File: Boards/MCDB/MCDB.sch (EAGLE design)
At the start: 60 parts, among them IC1 MC33926, IC2 MC33926, IC3 MC33926, IC4 MC33926, IC5 MC33926, IC6 MC33926

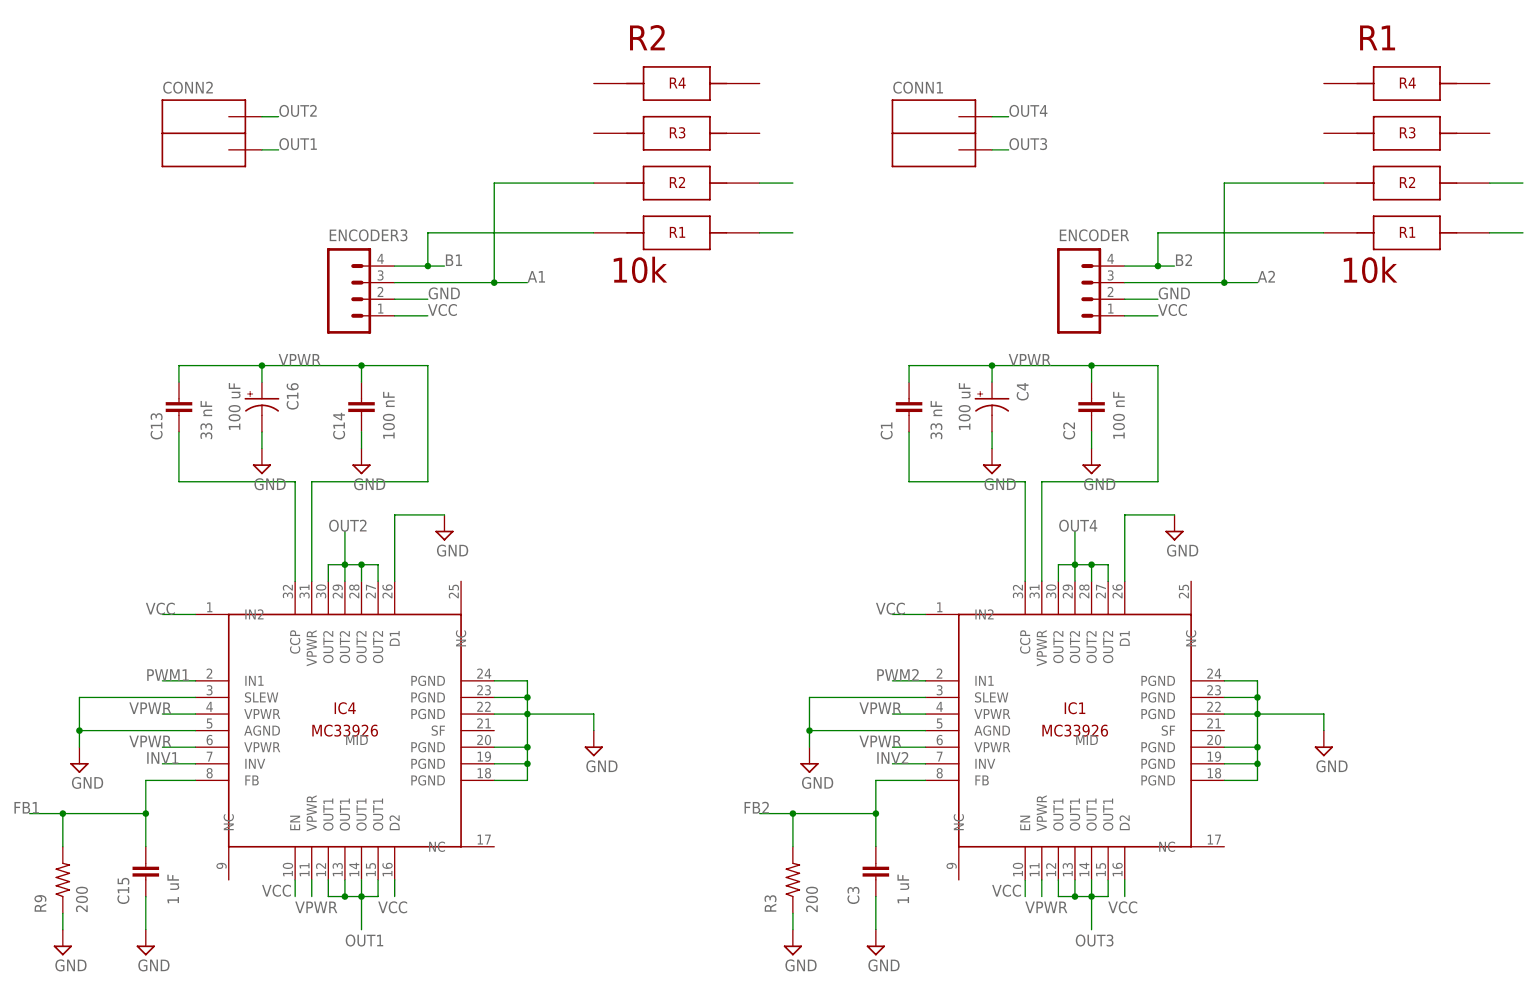
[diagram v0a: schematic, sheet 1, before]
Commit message: Started process of using new MC symbol
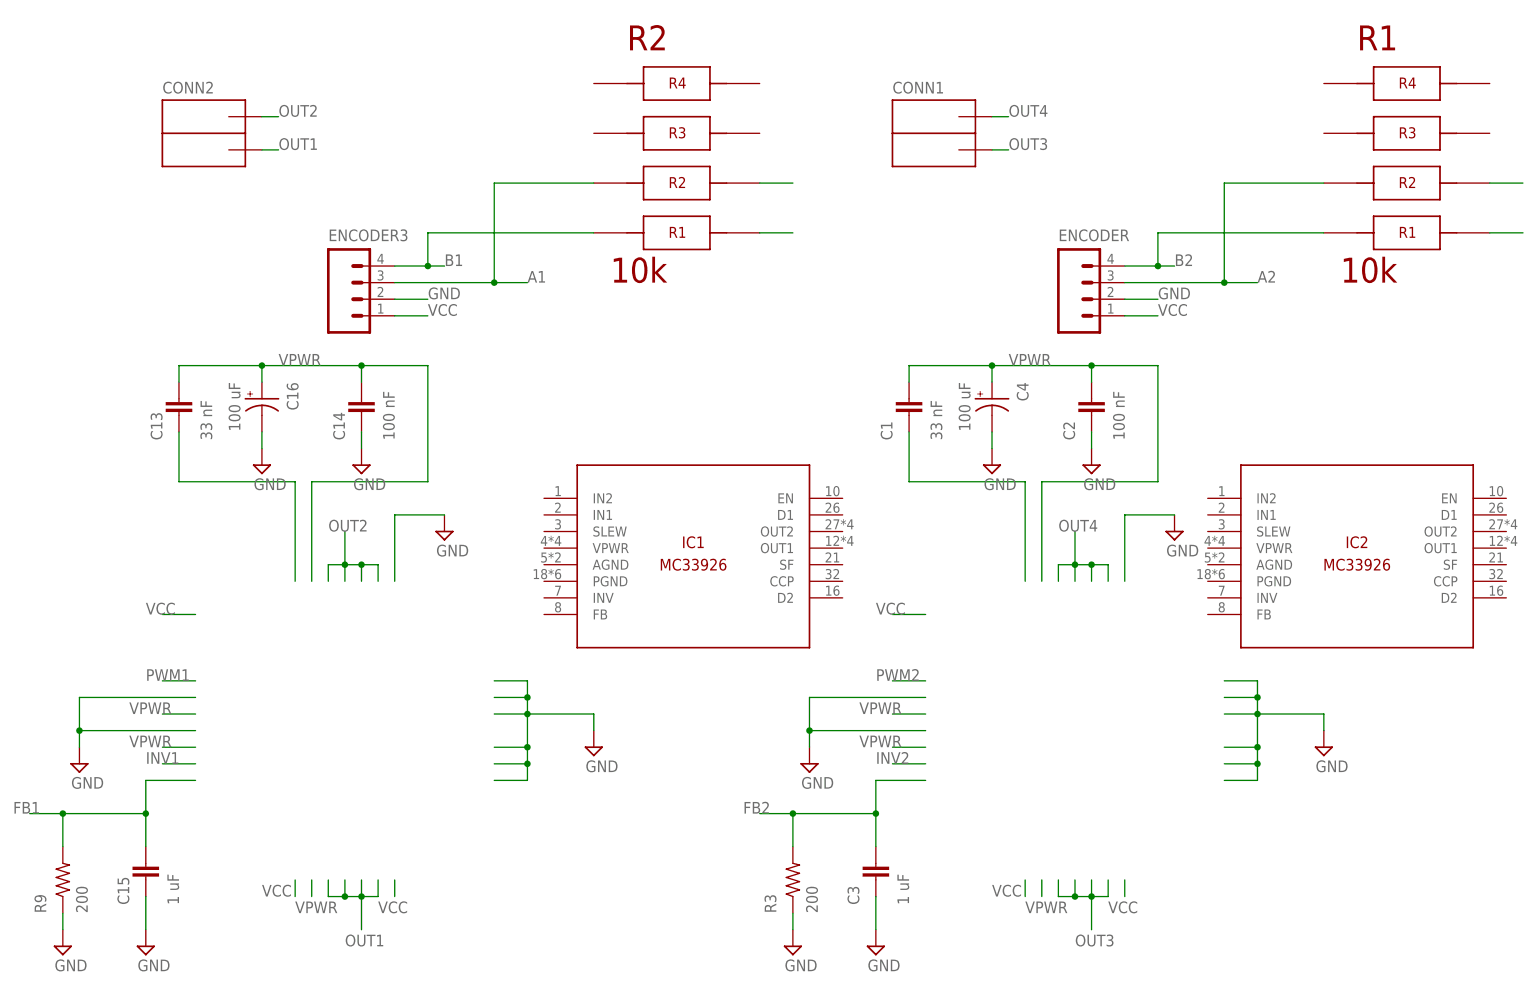
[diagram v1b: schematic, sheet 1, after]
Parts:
- removed IC3, IC4, IC5, IC6: MC33926, pie:MC33926
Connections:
- removed net INV1: IC4.INV
- removed net INV2: IC1.INV
- removed net INV3: IC2.INV
- removed net INV4: IC3.INV
- removed net INV5: IC5.INV
- removed net INV6: IC6.INV
- removed net PWM3: IC2.IN1
- removed net PWM4: IC3.IN1
- removed net PWM5: IC5.IN1
- removed net PWM6: IC6.IN1
- net CCP: no longer IC1.CCP
- net CCP1: no longer IC2.CCP
- net CCP2: no longer IC3.CCP
- net CCP3: no longer IC4.CCP
- net CCP4: no longer IC5.CCP
- net CCP5: no longer IC6.CCP
- net FB1: no longer IC4.FB
- net FB2: no longer IC1.FB
- net FB3: no longer IC2.FB
- net FB4: no longer IC3.FB
- net FB5: no longer IC5.FB
- net FB6: no longer IC6.FB
- net GND: no longer IC1.AGND, IC1.D1, IC1.PGND, IC1.PGND@1, IC1.PGND@2, IC1.PGND@3, IC1.PGND@4, IC1.PGND@5, IC1.SLEW, IC2.AGND, IC2.D1, IC2.PGND, IC2.PGND@1, IC2.PGND@2, IC2.PGND@3, IC2.PGND@4, IC2.PGND@5, IC2.SLEW, IC3.AGND, IC3.D1, IC3.PGND, IC3.PGND@1, IC3.PGND@2, IC3.PGND@3, IC3.PGND@4, IC3.PGND@5, IC3.SLEW, IC4.AGND, IC4.D1, IC4.PGND, IC4.PGND@1, IC4.PGND@2, IC4.PGND@3, IC4.PGND@4, IC4.PGND@5, IC4.SLEW, IC5.AGND, IC5.D1, IC5.PGND, IC5.PGND@1, IC5.PGND@2, IC5.PGND@3, IC5.PGND@4, IC5.PGND@5, IC5.SLEW, IC6.AGND, IC6.D1, IC6.PGND, IC6.PGND@1, IC6.PGND@2, IC6.PGND@3, IC6.PGND@4, IC6.PGND@5, IC6.SLEW
- net OUT1: no longer IC4.OUT1@1, IC4.OUT1@2, IC4.OUT1@3, IC4.OUT1@4
- net OUT10: no longer IC5.OUT2@1, IC5.OUT2@3, IC5.OUT2@4, IC5.OUT2@5
- net OUT11: no longer IC6.OUT1@1, IC6.OUT1@2, IC6.OUT1@3, IC6.OUT1@4
- net OUT12: no longer IC6.OUT2@1, IC6.OUT2@3, IC6.OUT2@4, IC6.OUT2@5
- net OUT2: no longer IC4.OUT2@1, IC4.OUT2@3, IC4.OUT2@4, IC4.OUT2@5
- net OUT3: no longer IC1.OUT1@1, IC1.OUT1@2, IC1.OUT1@3, IC1.OUT1@4
- net OUT4: no longer IC1.OUT2@1, IC1.OUT2@3, IC1.OUT2@4, IC1.OUT2@5
- net OUT5: no longer IC2.OUT1@1, IC2.OUT1@2, IC2.OUT1@3, IC2.OUT1@4
- net OUT6: no longer IC2.OUT2@1, IC2.OUT2@3, IC2.OUT2@4, IC2.OUT2@5
- net OUT7: no longer IC3.OUT1@1, IC3.OUT1@2, IC3.OUT1@3, IC3.OUT1@4
- net OUT8: no longer IC3.OUT2@1, IC3.OUT2@3, IC3.OUT2@4, IC3.OUT2@5
- net OUT9: no longer IC5.OUT1@1, IC5.OUT1@2, IC5.OUT1@3, IC5.OUT1@4
- net PWM1: no longer IC4.IN1
- net PWM2: no longer IC1.IN1
- net VCC: no longer IC1.D2, IC1.EN, IC1.IN2, IC2.D2, IC2.EN, IC2.IN2, IC3.D2, IC3.EN, IC3.IN2, IC4.D2, IC4.EN, IC4.IN2, IC5.D2, IC5.EN, IC5.IN2, IC6.D2, IC6.EN, IC6.IN2
- net VPWR: no longer IC1.VPWR, IC1.VPWR@1, IC1.VPWR@2, IC1.VPWR@3, IC2.VPWR, IC2.VPWR@1, IC2.VPWR@2, IC2.VPWR@3, IC3.VPWR, IC3.VPWR@1, IC3.VPWR@2, IC3.VPWR@3, IC4.VPWR, IC4.VPWR@1, IC4.VPWR@2, IC4.VPWR@3, IC5.VPWR, IC5.VPWR@1, IC5.VPWR@2, IC5.VPWR@3, IC6.VPWR, IC6.VPWR@1, IC6.VPWR@2, IC6.VPWR@3

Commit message: Started modifying motor controller board
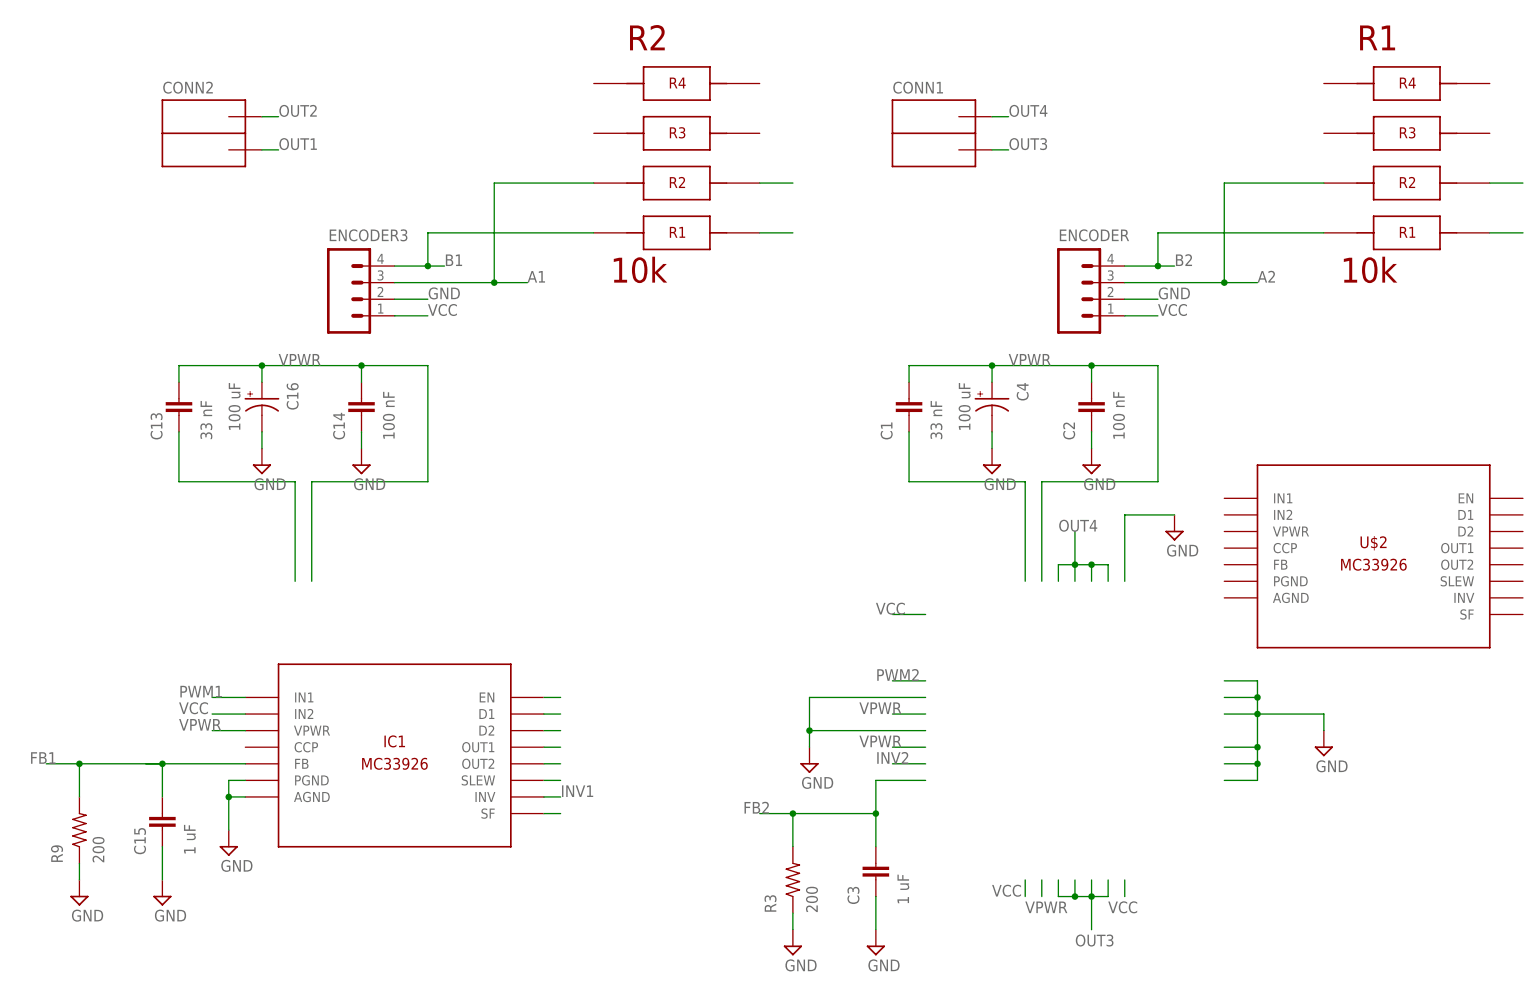
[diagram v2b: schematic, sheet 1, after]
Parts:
- removed IC2: MC33926, pie:MC33926
- added U$2, U$3, U$4, U$5, U$6: MC33926, pie:MC33926
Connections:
- new net INV1: IC1.INV
- new net N$10: IC1.SLEW
- new net N$11: IC1.SF
- new net N$2: IC1.EN
- new net N$3: IC1.D1
- new net N$6: IC1.D2
- new net N$8: IC1.OUT1
- new net N$9: IC1.OUT2
- net FB1: now also IC1.FB
- net GND: now also IC1.AGND, IC1.PGND
- net PWM1: now also IC1.IN1
- net VCC: now also IC1.IN2
- net VPWR: now also IC1.VPWR
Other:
- moved on the sheet: C15, R9

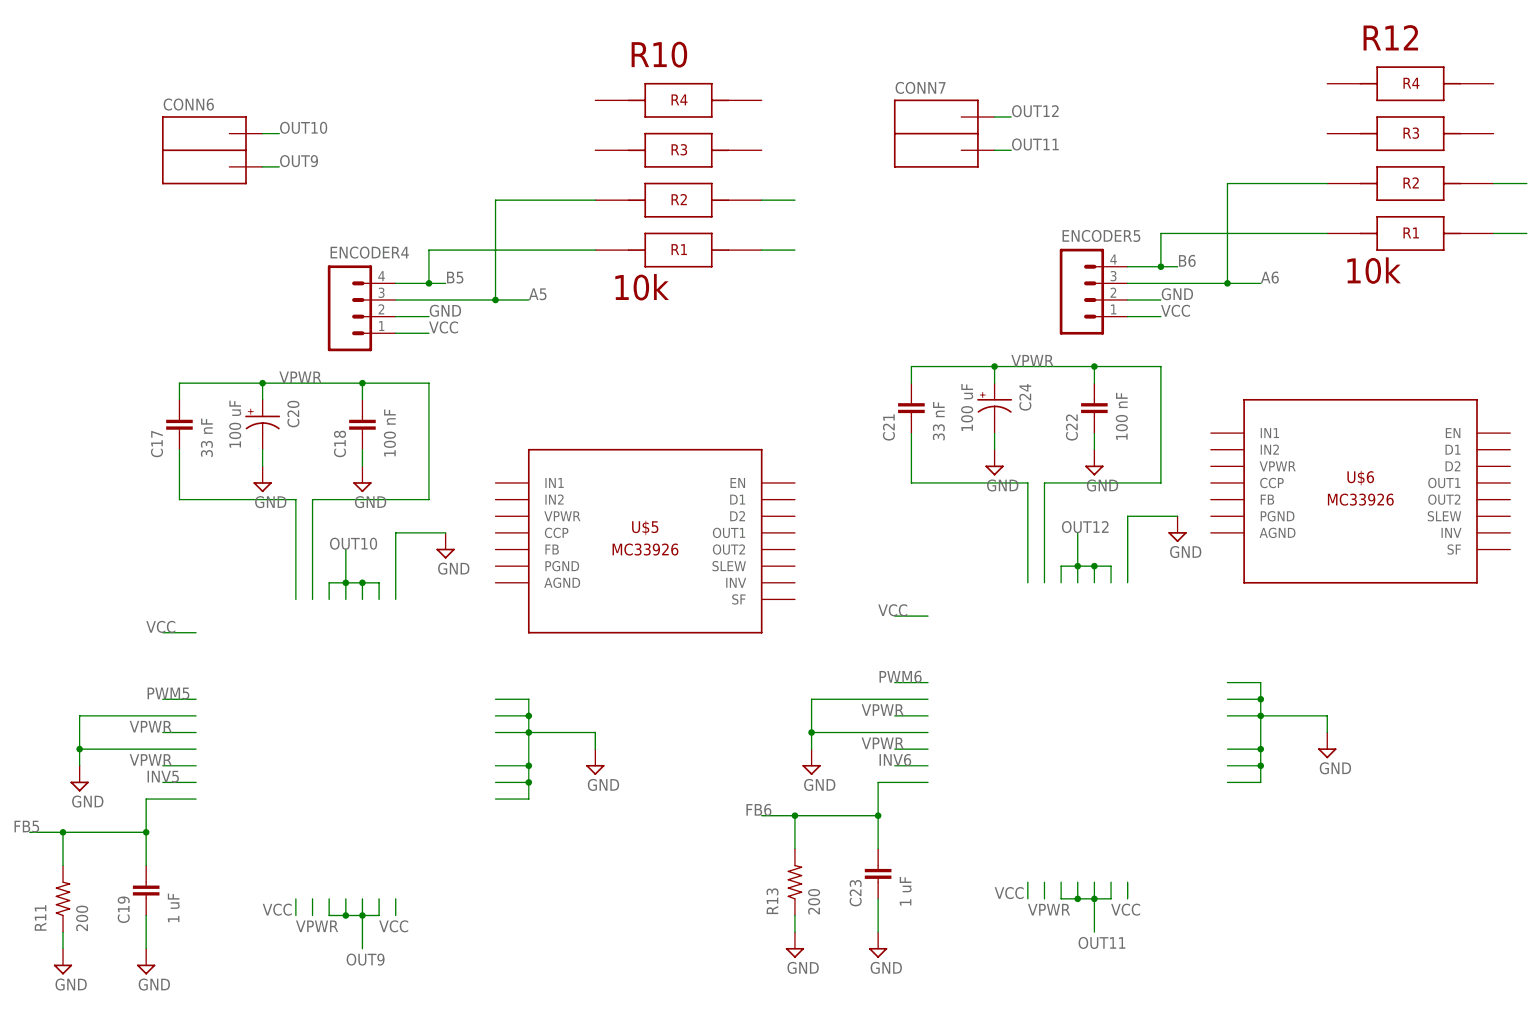
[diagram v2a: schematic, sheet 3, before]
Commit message: edited to accomodate new symbol
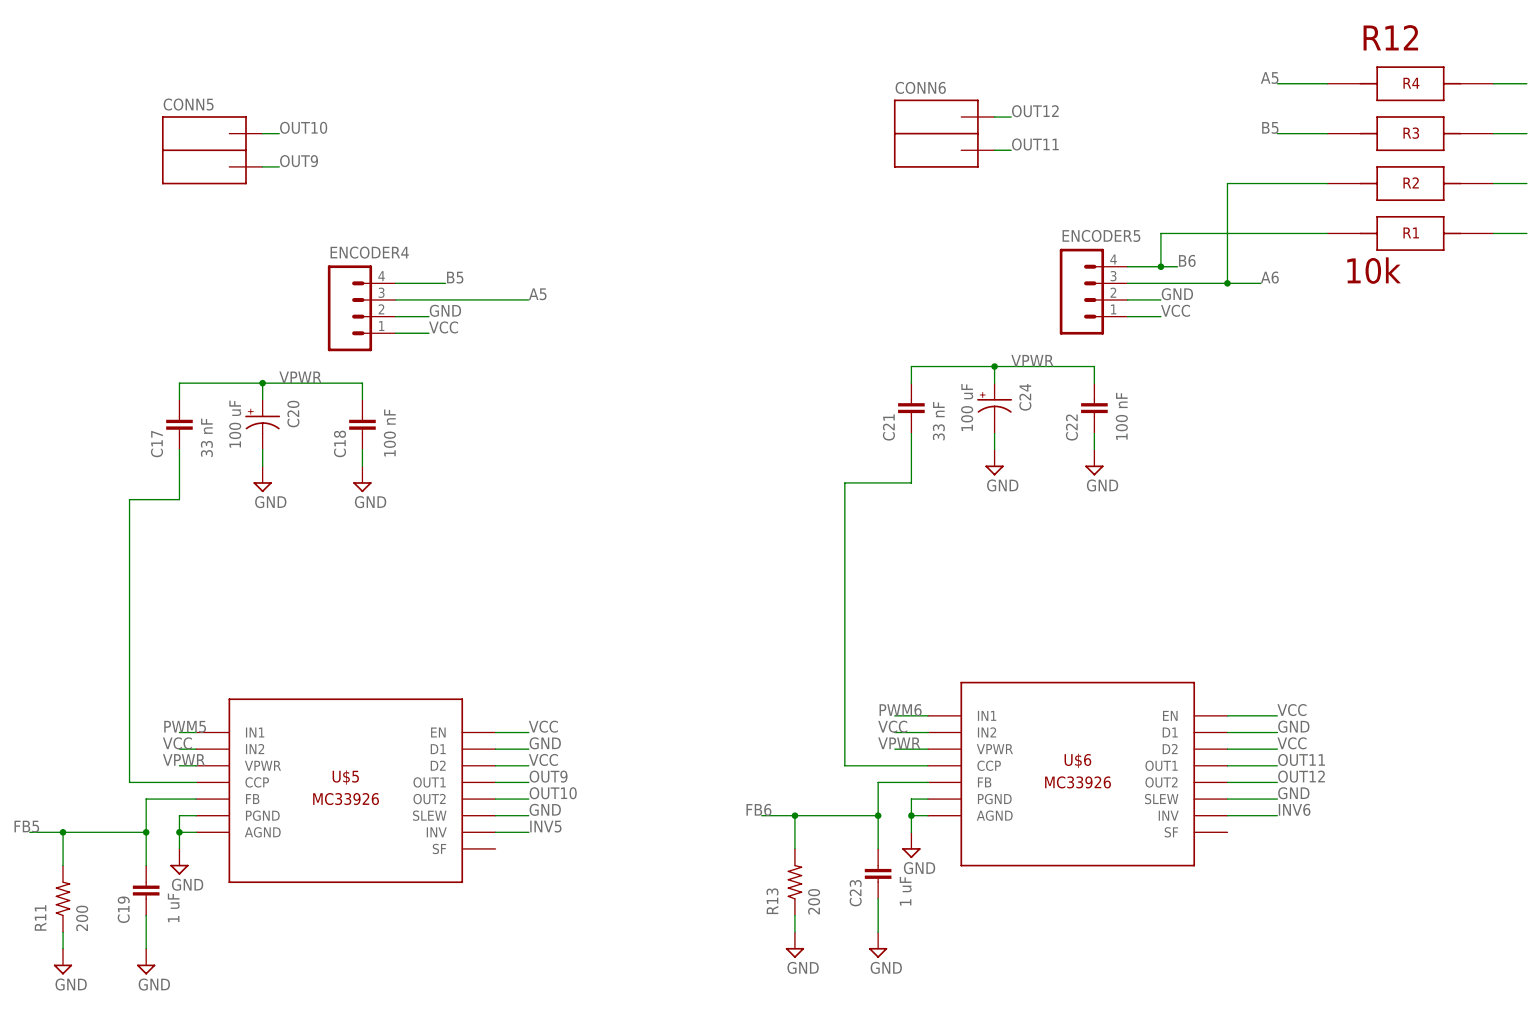
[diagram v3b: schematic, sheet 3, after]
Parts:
- removed R10, R2, R4: 10k, pie:4X-0603
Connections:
- removed net CCP2: C9.1
- removed net CCP4: C17.1
- removed net CCP5: C21.1
- new net INV2: U$2.INV
- new net INV3: U$3.INV
- new net INV4: U$4.INV
- new net INV5: U$5.INV
- new net INV6: U$6.INV
- new net N$1: C21.1, U$6.CCP
- new net N$14: R12.3
- new net N$15: R12.4
- new net N$20: C9.1, U$4.CCP
- new net PWM3: U$3.IN1
- new net PWM4: U$4.IN1
- new net PWM5: U$5.IN1
- new net PWM6: U$6.IN1
- net A1: now also R1.5; no longer R2.7
- net A3: now also R6.5; no longer R4.7
- net A5: now also R12.5; no longer R10.7
- net B1: now also R1.6; no longer R2.8
- net B3: now also R6.6; no longer R4.8
- net B5: now also R12.6; no longer R10.8
- net CCP: now also U$2.CCP
- net CCP1: now also U$3.CCP
- net CCP3: now also IC1.CCP
- net FB2: now also U$2.FB
- net FB3: now also U$3.FB
- net FB4: now also U$4.FB
- net FB5: now also U$5.FB
- net FB6: now also U$6.FB
- net GND: now also CONN7.OUTA, IC1.D1, IC1.SLEW, U$2.AGND, U$2.D1, U$2.PGND, U$2.SLEW, U$3.AGND, U$3.D1, U$3.PGND, U$3.SLEW, U$4.AGND, U$4.D1, U$4.PGND, U$4.SLEW, U$5.AGND, U$5.D1, U$5.PGND, U$5.SLEW, U$6.AGND, U$6.D1, U$6.PGND, U$6.SLEW; no longer CONN5.OUTA
- net N$10: now also R6.4; no longer IC1.SLEW
- net N$2: now also R1.3; no longer IC1.EN
- net N$3: now also R1.4; no longer IC1.D1
- net N$6: now also C5.2, C6.2, C8.+; no longer IC1.D2
- net N$8: now also C17.1, U$5.CCP; no longer IC1.OUT1
- net N$9: now also R6.3; no longer IC1.OUT2
- net OUT1: now also CONN1.OUTB, IC1.OUT1; no longer CONN2.OUTB
- net OUT10: now also CONN5.OUTA, U$5.OUT2; no longer CONN6.OUTA
- net OUT11: now also CONN6.OUTB, U$6.OUT1; no longer CONN7.OUTB
- net OUT12: now also CONN6.OUTA, U$6.OUT2; no longer CONN7.OUTA
- net OUT2: now also CONN1.OUTA, IC1.OUT2; no longer CONN2.OUTA
- net OUT3: now also CONN2.OUTB, U$2.OUT1; no longer CONN1.OUTB
- net OUT4: now also CONN2.OUTA, U$2.OUT2; no longer CONN1.OUTA
- net OUT5: now also U$3.OUT1
- net OUT6: now also U$3.OUT2
- net OUT7: now also U$4.OUT1
- net OUT8: now also U$4.OUT2
- net OUT9: now also CONN5.OUTB, U$5.OUT1; no longer CONN6.OUTB
- net PWM2: now also U$2.IN1
- net VCC: now also IC1.D2, IC1.EN, U$2.D2, U$2.EN, U$2.IN2, U$3.D2, U$3.EN, U$3.IN2, U$4.D2, U$4.EN, U$4.IN2, U$5.D2, U$5.EN, U$5.IN2, U$6.D2, U$6.EN, U$6.IN2; no longer R10.1, R10.2, R2.1, R2.2, R4.1, R4.2
- net VPWR: now also CONN7.OUTB, U$2.VPWR, U$3.VPWR, U$4.VPWR, U$5.VPWR, U$6.VPWR; no longer C5.2, C6.2, C8.+, CONN5.OUTB
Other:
- moved on the sheet: CONN1, CONN2, CONN6, U$2, U$3, U$4, U$5, U$6
